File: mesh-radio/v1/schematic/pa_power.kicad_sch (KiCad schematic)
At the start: 28 parts, among them Q3 SSM3K56ACT, U13 TPS2121RUXR, U14 TPS63810YFFR, U15 TLV75528PDQNR, U16 TMP1075NDRLR

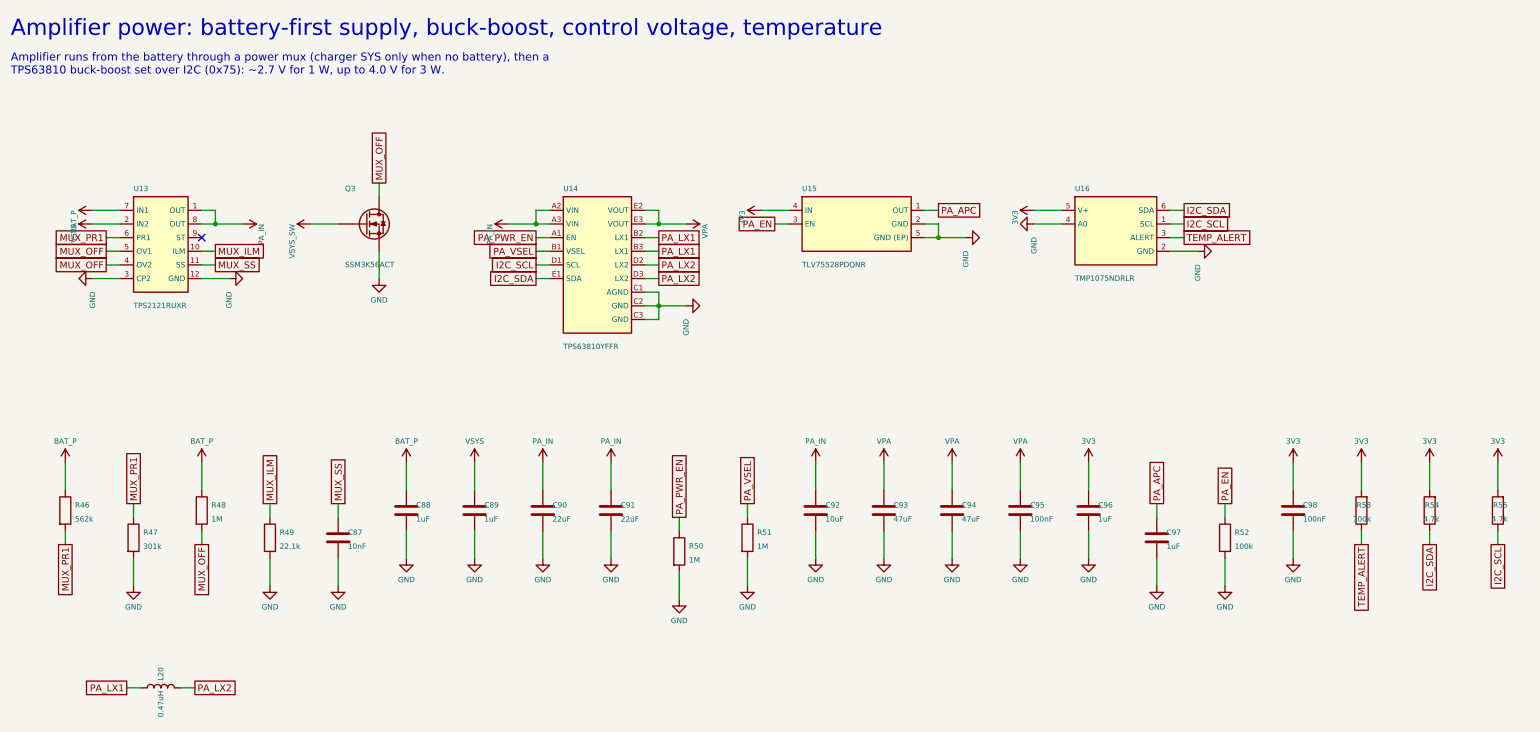
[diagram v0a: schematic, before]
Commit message: Mesh Radio v1: fix every design-review finding, add the part audit
An independent review of the schematic found two critical and nine further
issues; all are fixed in src/circuit.py:
- reverse-battery FET gate now returns to the cell's own minus terminal, so
  a backwards cell stays isolated even while USB/solar/drone power the board
- solar and drone inputs: reverse-blocking Schottky + 22 V flat-clamp TVS
  (the 15 V TVS would have failed on a 12 V panel); 4.7 V clamp on every
  eFuse EN/UVLO pin so 20 V on an input stays inside its rating
- ideal diode (LM66100) holds VSYS on the cell when a 3 W burst trips the
  charger's 3.0 V battery disconnect
- charge LED moved to STAT2 (charging), USB cut-off lowered to 5.4 V,
  charger /CE on a GPIO for firmware temperature control, -40 C TCXO,
  power mux on only with the amplifier, header VSYS pin removed
- firmware ceilings documented: SX1262 +20 dBm, amplifier 3.6 V by default

docs/part-audit.md: all 125 lines checked at DigiKey and LCSC (genuine
LCSC numbers, DigiKey numbers, second sources for out-of-stock lines);
parts cost about $76 at 10 boards, $58 at 100.

Schematic regenerated: ERC 0 violations, netlist equals circuit.py.

Co-Authored-By: Claude Opus 5.5 <noreply@anthropic.com>
Claude-Session: https://claude.ai/code/session_015TBB2ThqxHSgA8MkFosmn9
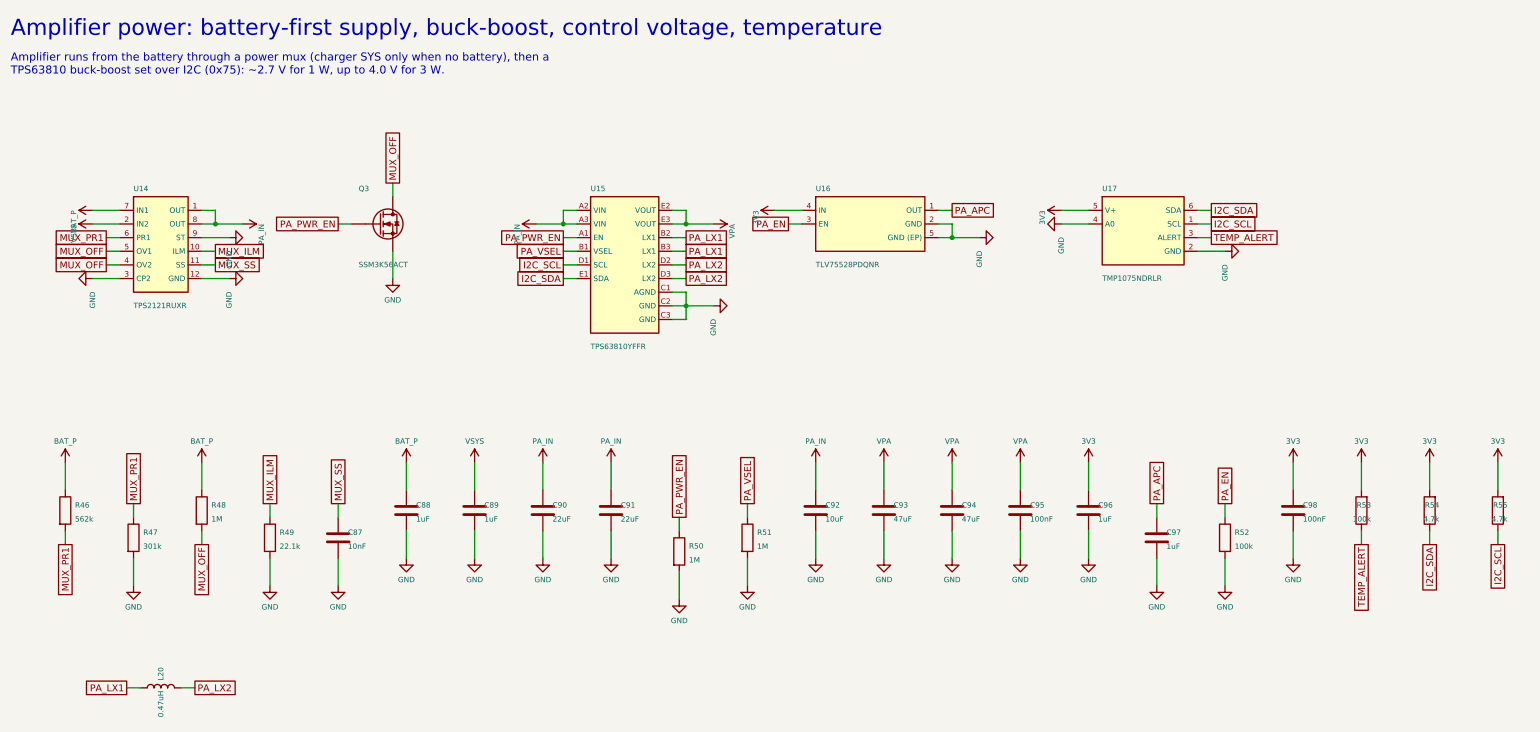
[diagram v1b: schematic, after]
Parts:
- removed U13: TPS2121RUXR, og:VQFN-12_TPS2121RUX, symbol og:TPS2121
- added U17: TMP1075NDRLR, og:SOT-563_L1.6-W1.2-P0.50-LS1.6-BR, symbol og:TMP1075
- C87: DigiKey (none) -> 1276-1028-1-ND
- C88, C89: DigiKey (none) -> 1276-1184-1-ND
- C90, C91: LCSC C45783 -> C86817; MPN CL21A226MAQNNNE -> GRM21BR61C226ME44L; Manufacturer Samsung Electro-Mechanics -> Murata
- C92: DigiKey (none) -> 1276-2891-1-ND
- C93, C94: DigiKey (none) -> 1276-1852-1-ND
- C95, C98: DigiKey (none) -> 1276-1001-1-ND
- C96, C97: DigiKey (none) -> 1276-1067-1-ND
- L20: DigiKey (none) -> 490-13049-1-ND
- Q3: DigiKey (none) -> SSM3K56ACTL3FCT-ND
- R46: DigiKey (none) -> 311-562KLRCT-ND
- R47: DigiKey (none) -> 311-301KLRCT-ND
- R48, R50, R51: DigiKey (none) -> 311-1.00MLRCT-ND
- R49: DigiKey (none) -> 311-22.1KLRCT-ND
- R52, R53: DigiKey (none) -> 311-100KLRCT-ND
- R54, R55: DigiKey (none) -> 311-4.7KLRCT-ND
- U14: value TPS63810YFFR -> TPS2121RUXR; footprint og:DSBGA-15_L2.2-W1.4-R3-V5-P0.40-BL -> og:VQFN-12_TPS2121RUX; symbol og:TPS63810 -> og:TPS2121; DigiKey (none) -> 296-53410-1-ND; LCSC C1852139 -> C485916; MPN TPS63810YFFR -> TPS2121RUXR
- U15: value TLV75528PDQNR -> TPS63810YFFR; footprint og:X2SON-4_L1.0-W1.0-P0.65-TL-EP -> og:DSBGA-15_L2.2-W1.4-R3-V5-P0.40-BL; symbol og:TLV75528 -> og:TPS63810; DigiKey (none) -> 296-TPS63810YFFRCT-ND; LCSC C2865384 -> C1852139; MPN TLV75528PDQNR -> TPS63810YFFR
- U16: value TMP1075NDRLR -> TLV75528PDQNR; footprint og:SOT-563_L1.6-W1.2-P0.50-LS1.6-BR -> og:X2SON-4_L1.0-W1.0-P0.65-TL-EP; symbol og:TMP1075 -> og:TLV75528; DigiKey (none) -> 296-TLV75528PDQNRCT-ND; LCSC C3663690 -> C2865384; MPN TMP1075NDRLR -> TLV75528PDQNR
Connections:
- net VSYS_SW is gone; now on net PA_PWR_EN: Q3.1 (G)
- net 3V3: now also U16.4 (IN), U17.5 (V+); no longer U15.4 (IN), U16.5 (V+)
- net BAT_P: now also U14.7 (IN1)
- net GND: now also U14.12 (GND), U14.3 (CP2), U14.9 (ST), U15.C1 (AGND), U15.C2 (GND), U15.C3 (GND), U16.5 (GND (EP)), U17.2 (GND), U17.4 (A0); no longer U14.C1 (AGND), U14.C2 (GND), U14.C3 (GND), U15.2 (GND), U15.5 (GND (EP)), U16.4 (A0)
- net I2C_SCL: now also U15.D1 (SCL), U17.1 (SCL); no longer U14.D1 (SCL), U16.1 (SCL)
- net I2C_SDA: now also U15.E1 (SDA), U17.6 (SDA); no longer U14.E1 (SDA), U16.6 (SDA)
- net MUX_ILM: now also U14.10 (ILM)
- net MUX_OFF: now also U14.4 (OV2), U14.5 (OV1)
- net MUX_PR1: now also U14.6 (PR1)
- net MUX_SS: now also U14.11 (SS)
- net PA_APC: now also U16.1 (OUT); no longer U15.1 (OUT)
- net PA_EN: now also U16.3 (EN); no longer U15.3 (EN)
- net PA_IN: now also U14.1 (OUT), U14.8 (OUT), U15.A2 (VIN), U15.A3 (VIN); no longer U14.A2 (VIN), U14.A3 (VIN)
- net PA_LX1: now also U15.B2 (LX1), U15.B3 (LX1); no longer U14.B2 (LX1), U14.B3 (LX1)
- net PA_LX2: now also U15.D2 (LX2), U15.D3 (LX2); no longer U14.D2 (LX2), U14.D3 (LX2)
- net PA_PWR_EN: now also U15.A1 (EN); no longer U14.A1 (EN)
- net PA_VSEL: now also U15.B1 (VSEL); no longer U14.B1 (VSEL)
- net TEMP_ALERT: now also U17.3 (ALERT); no longer U16.3 (ALERT)
- net VPA: now also U15.E2 (VOUT), U15.E3 (VOUT); no longer U14.E2 (VOUT), U14.E3 (VOUT)
- net VSYS: now also U14.2 (IN2)
- no-connect marks 1 -> 0
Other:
- moved on the sheet: Q3

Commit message: Mesh radio v1: LFCG-1000+ antenna filter; missing-antenna detector
Owner decisions of 19 Oct: keep 3 W with the heat fixes and a gap pad to
a metal enclosure, 6 layers, 300 mA charging, new parts at the designer's
judgement.  This commit, from sim/rf:
- FL1 LFCN-1000+ (1206) -> LFCG-1000+ (0805, 8 pads, Mini-Circuits case
  GE0805C-2: in 8, out 4): no stop-band re-entry at 5.5-10 GHz, where the
  3 W 6th-10th harmonics failed FCC's restricted-band limit;
- a reflected-wave detector: a printed line beside the ANT line
  terminated in 49.9 R, an Infineon BAT15-02EL, 1 nF and 100 k into
  P0.30/AIN6, so firmware can cut the amplifier within ~1 ms of a packet
  with no antenna (the antenna switch sees 109-160 % of its rating then);
- P0.31/AIN7 reads the charger's NTC (firmware's 0-45 C charging rule);
  the expansion header's IO3/IO4 give way (four spare pins remain).
ERC 0, netlist equals circuit.py, every pin and pad accounted for.

Co-Authored-By: Claude Opus 5.5 <noreply@anthropic.com>
Claude-Session: https://claude.ai/code/session_015TBB2ThqxHSgA8MkFosmn9
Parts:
- removed C87: 10nF, og:C_0402, symbol Device:C
- removed R46: 562k, og:R_0402, symbol Device:R
- removed R47: 301k, og:R_0402, symbol Device:R
- added C99: 100nF, og:C_0402, symbol Device:C
- added R56, R57: 4.7k, og:R_0402, symbol Device:R
- C88: value 1uF -> 10nF; footprint og:C_0603 -> og:C_0402; DigiKey 1276-1184-1-ND -> 1276-1028-1-ND; LCSC C29936 -> C15195; MPN CL10B105KA8NNNC -> CL05B103KB5NNNC
- C90: value 22uF -> 1uF; footprint og:C_0805 -> og:C_0603; DigiKey (none) -> 1276-1184-1-ND; LCSC C86817 -> C29936; MPN GRM21BR61C226ME44L -> CL10B105KA8NNNC; Manufacturer Murata -> Samsung Electro-Mechanics
- C92: value 10uF -> 22uF; DigiKey 1276-2891-1-ND -> (none); LCSC C15850 -> C86817; MPN CL21A106KAYNNNE -> GRM21BR61C226ME44L; Manufacturer Samsung Electro-Mechanics -> Murata
- C93: value 47uF -> 10uF; DigiKey 1276-1852-1-ND -> 1276-2891-1-ND; LCSC C16780 -> C15850; MPN CL21A476MQYNNNE -> CL21A106KAYNNNE
- C95: value 100nF -> 47uF; footprint og:C_0402 -> og:C_0805; DigiKey 1276-1001-1-ND -> 1276-1852-1-ND; LCSC C1525 -> C16780; MPN CL05B104KO5NNNC -> CL21A476MQYNNNE
- C96: value 1uF -> 100nF; DigiKey 1276-1067-1-ND -> 1276-1001-1-ND; LCSC C29266 -> C1525; MPN CL05A105KO5NNNC -> CL05B104KO5NNNC
- C98: value 100nF -> 1uF; DigiKey 1276-1001-1-ND -> 1276-1067-1-ND; LCSC C1525 -> C29266; MPN CL05B104KO5NNNC -> CL05A105KO5NNNC
- R48: value 1M -> 562k; DigiKey 311-1.00MLRCT-ND -> 311-562KLRCT-ND; LCSC C138033 -> C273337; MPN RC0402FR-071ML -> RC0402FR-07562KL
- R49: value 22.1k -> 301k; DigiKey 311-22.1KLRCT-ND -> 311-301KLRCT-ND; LCSC C163478 -> C171693; MPN RC0402FR-0722K1L -> RC0402FR-07301KL
- R51: value 1M -> 22.1k; DigiKey 311-1.00MLRCT-ND -> 311-22.1KLRCT-ND; LCSC C138033 -> C163478; MPN RC0402FR-071ML -> RC0402FR-0722K1L
- R52, R53: value 100k -> 1M; DigiKey 311-100KLRCT-ND -> 311-1.00MLRCT-ND; LCSC C60491 -> C138033; MPN RC0402FR-07100KL -> RC0402FR-071ML
- R54, R55: value 4.7k -> 100k; DigiKey 311-4.7KLRCT-ND -> 311-100KLRCT-ND; LCSC C105871 -> C60491; MPN RC0402FR-074K7L -> RC0402FR-07100KL
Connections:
- net 3V3: now also C97.1, C99.1, R56.2, R57.2; no longer C96.1, C98.1, R53.2, R54.2
- net BAT_P: now also C89.1, R50.1; no longer C88.1
- net GND: now also R53.2, R54.2, C99.2; no longer R50.2
- net I2C_SCL: now also R57.1; no longer R55.1
- net I2C_SDA: now also R56.1; no longer R54.1
- net MUX_ILM: now also R51.1; no longer R49.1
- net MUX_OFF: now also R50.2; no longer R48.2
- net MUX_PR1: now also R48.2, R49.1
- net MUX_SS: now also C88.1
- net PA_APC: now also C98.1; no longer C97.1
- net PA_EN: now also R54.1; no longer R52.1
- net PA_IN: now also C93.1; no longer C90.1
- net PA_PWR_EN: now also R52.1; no longer R50.1
- net PA_VSEL: now also R53.1; no longer R51.1
- net TEMP_ALERT: now also R55.1; no longer R53.1
- net VPA: now also C96.1; no longer C93.1
- net VSYS: now also C90.1; no longer C89.1
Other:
- moved on the sheet: C88, C89, C90, C91, C92, C93, C94, C95, C96, C97, C98, R48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
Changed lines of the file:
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@@
 		(on_board yes)
 		(dnp no)
-		(property "Reference" "R46"
+		(property "Reference" "R48"
 			(at 27.2 103.14 0)
 			(effects
@@
 			(project "mesh-radio"
 				(path "/1e0df660-60b5-6ed0-6a2a-f5098e72ebfd/2b2c8bd9-9e70-fab2-afb8-de35f83d5714"
-					(reference "R46")
+					(reference "R48")
 					(unit 1)
 				)
@@
 		(on_board yes)
 		(dnp no)
-		(property "Reference" "R47"
+		(property "Reference" "R49"
 			(at 39.9 108.22 0)
 			(effects
@@
 			(project "mesh-radio"
 				(path "/1e0df660-60b5-6ed0-6a2a-f5098e72ebfd/2b2c8bd9-9e70-fab2-afb8-de35f83d5714"
-					(reference "R47")
+					(reference "R49")
 					(unit 1)
 				)
@@
 		(on_board yes)
 		(dnp no)
-		(property "Reference" "R48"
+		(property "Reference" "R50"
 			(at 52.6 103.14 0)
 			(effects
@@
 			(project "mesh-radio"
 				(path "/1e0df660-60b5-6ed0-6a2a-f5098e72ebfd/2b2c8bd9-9e70-fab2-afb8-de35f83d5714"
-					(reference "R48")
+					(reference "R50")
 					(unit 1)
 				)
@@
 		(on_board yes)
 		(dnp no)
-		(property "Reference" "R49"
+		(property "Reference" "R51"
 			(at 65.3 108.22 0)
 			(effects
@@
 			(project "mesh-radio"
 				(path "/1e0df660-60b5-6ed0-6a2a-f5098e72ebfd/2b2c8bd9-9e70-fab2-afb8-de35f83d5714"
-					(reference "R49")
+					(reference "R51")
 					(unit 1)
 				)
@@
 		(on_board yes)
 		(dnp no)
-		(property "Reference" "C87"
+		(property "Reference" "C88"
 			(at 78 108.22 0)
 			(effects
@@
 			(project "mesh-radio"
 				(path "/1e0df660-60b5-6ed0-6a2a-f5098e72ebfd/2b2c8bd9-9e70-fab2-afb8-de35f83d5714"
-					(reference "C87")
+					(reference "C88")
 					(unit 1)
 				)
@@
 		(on_board yes)
 		(dnp no)
-		(property "Reference" "C88"
+		(property "Reference" "C89"
 			(at 90.7 103.14 0)
 			(effects
@@
 			(project "mesh-radio"
 				(path "/1e0df660-60b5-6ed0-6a2a-f5098e72ebfd/2b2c8bd9-9e70-fab2-afb8-de35f83d5714"
-					(reference "C88")
+					(reference "C89")
 					(unit 1)
 				)
@@
 		(on_board yes)
 		(dnp no)
-		(property "Reference" "C89"
+		(property "Reference" "C90"
 			(at 103.4 103.14 0)
 			(effects
@@
 			(project "mesh-radio"
 				(path "/1e0df660-60b5-6ed0-6a2a-f5098e72ebfd/2b2c8bd9-9e70-fab2-afb8-de35f83d5714"
-					(reference "C89")
+					(reference "C90")
 					(unit 1)
 				)
@@
 		(on_board yes)
 		(dnp no)
-		(property "Reference" "C90"
+		(property "Reference" "C91"
 			(at 116.1 103.14 0)
 			(effects
@@
 			(project "mesh-radio"
 				(path "/1e0df660-60b5-6ed0-6a2a-f5098e72ebfd/2b2c8bd9-9e70-fab2-afb8-de35f83d5714"
-					(reference "C90")
+					(reference "C91")
 					(unit 1)
 				)
@@
 		(on_board yes)
 		(dnp no)
-		(property "Reference" "C91"
+		(property "Reference" "C92"
 			(at 128.8 103.14 0)
 			(effects
@@
 			(project "mesh-radio"
 				(path "/1e0df660-60b5-6ed0-6a2a-f5098e72ebfd/2b2c8bd9-9e70-fab2-afb8-de35f83d5714"
-					(reference "C91")
+					(reference "C92")
 					(unit 1)
 				)
@@
 		(on_board yes)
 		(dnp no)
-		(property "Reference" "R50"
+		(property "Reference" "R52"
 			(at 141.5 110.76 0)
 			(effects
@@
 			(project "mesh-radio"
 				(path "/1e0df660-60b5-6ed0-6a2a-f5098e72ebfd/2b2c8bd9-9e70-fab2-afb8-de35f83d5714"
-					(reference "R50")
+					(reference "R52")
 					(unit 1)
 				)
@@
 		(on_board yes)
 		(dnp no)
-		(property "Reference" "R51"
+		(property "Reference" "R53"
 			(at 154.2 108.22 0)
 			(effects
@@
 			(project "mesh-radio"
 				(path "/1e0df660-60b5-6ed0-6a2a-f5098e72ebfd/2b2c8bd9-9e70-fab2-afb8-de35f83d5714"
-					(reference "R51")
+					(reference "R53")
 					(unit 1)
 				)
@@
 		(on_board yes)
 		(dnp no)
-		(property "Reference" "C92"
+		(property "Reference" "C93"
 			(at 166.9 103.14 0)
 			(effects
@@
 			(project "mesh-radio"
 				(path "/1e0df660-60b5-6ed0-6a2a-f5098e72ebfd/2b2c8bd9-9e70-fab2-afb8-de35f83d5714"
-					(reference "C92")
+					(reference "C93")
 					(unit 1)
 				)
@@
 		(on_board yes)
 		(dnp no)
-		(property "Reference" "C93"
+		(property "Reference" "C94"
 			(at 179.6 103.14 0)
 			(effects
@@
 			(project "mesh-radio"
 				(path "/1e0df660-60b5-6ed0-6a2a-f5098e72ebfd/2b2c8bd9-9e70-fab2-afb8-de35f83d5714"
-					(reference "C93")
+					(reference "C94")
 					(unit 1)
 				)
@@
 		(on_board yes)
 		(dnp no)
-		(property "Reference" "C94"
+		(property "Reference" "C95"
 			(at 192.3 103.14 0)
 			(effects
@@
 			(project "mesh-radio"
 				(path "/1e0df660-60b5-6ed0-6a2a-f5098e72ebfd/2b2c8bd9-9e70-fab2-afb8-de35f83d5714"
-					(reference "C94")
+					(reference "C95")
 					(unit 1)
 				)
@@
 		(on_board yes)
 		(dnp no)
-		(property "Reference" "C95"
+		(property "Reference" "C96"
 			(at 205 103.14 0)
 			(effects
@@
 			(project "mesh-radio"
 				(path "/1e0df660-60b5-6ed0-6a2a-f5098e72ebfd/2b2c8bd9-9e70-fab2-afb8-de35f83d5714"
-					(reference "C95")
+					(reference "C96")
 					(unit 1)
 				)
@@
 		(on_board yes)
 		(dnp no)
-		(property "Reference" "C96"
+		(property "Reference" "C97"
 			(at 217.7 103.14 0)
 			(effects
@@
 			(project "mesh-radio"
 				(path "/1e0df660-60b5-6ed0-6a2a-f5098e72ebfd/2b2c8bd9-9e70-fab2-afb8-de35f83d5714"
-					(reference "C96")
+					(reference "C97")
 					(unit 1)
 				)
@@
 		(on_board yes)
 		(dnp no)
-		(property "Reference" "C97"
+		(property "Reference" "C98"
 			(at 230.4 108.22 0)
 			(effects
@@
 			(project "mesh-radio"
 				(path "/1e0df660-60b5-6ed0-6a2a-f5098e72ebfd/2b2c8bd9-9e70-fab2-afb8-de35f83d5714"
-					(reference "C97")
+					(reference "C98")
 					(unit 1)
 				)
@@
 		(on_board yes)
 		(dnp no)
-		(property "Reference" "R52"
+		(property "Reference" "R54"
 			(at 243.1 108.22 0)
 			(effects
@@
 			(project "mesh-radio"
 				(path "/1e0df660-60b5-6ed0-6a2a-f5098e72ebfd/2b2c8bd9-9e70-fab2-afb8-de35f83d5714"
-					(reference "R52")
+					(reference "R54")
 					(unit 1)
 				)
@@
 		(on_board yes)
 		(dnp no)
-		(property "Reference" "C98"
+		(property "Reference" "C99"
 			(at 255.8 103.14 0)
 			(effects
@@
 			(project "mesh-radio"
 				(path "/1e0df660-60b5-6ed0-6a2a-f5098e72ebfd/2b2c8bd9-9e70-fab2-afb8-de35f83d5714"
-					(reference "C98")
+					(reference "C99")
 					(unit 1)
 				)
@@
 		(on_board yes)
 		(dnp no)
-		(property "Reference" "R53"
+		(property "Reference" "R55"
 			(at 268.5 103.14 0)
 			(effects
@@
 			(project "mesh-radio"
 				(path "/1e0df660-60b5-6ed0-6a2a-f5098e72ebfd/2b2c8bd9-9e70-fab2-afb8-de35f83d5714"
-					(reference "R53")
+					(reference "R55")
 					(unit 1)
 				)
@@
 		(on_board yes)
 		(dnp no)
-		(property "Reference" "R54"
+		(property "Reference" "R56"
 			(at 281.2 103.14 0)
 			(effects
@@
 			(project "mesh-radio"
 				(path "/1e0df660-60b5-6ed0-6a2a-f5098e72ebfd/2b2c8bd9-9e70-fab2-afb8-de35f83d5714"
-					(reference "R54")
+					(reference "R56")
 					(unit 1)
 				)
@@
 		(on_board yes)
 		(dnp no)
-		(property "Reference" "R55"
+		(property "Reference" "R57"
 			(at 293.9 103.14 0)
 			(effects
@@
 			(project "mesh-radio"
 				(path "/1e0df660-60b5-6ed0-6a2a-f5098e72ebfd/2b2c8bd9-9e70-fab2-afb8-de35f83d5714"
-					(reference "R55")
+					(reference "R57")
 					(unit 1)
 				)
